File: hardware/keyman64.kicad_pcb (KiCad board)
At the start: 2 copper layers, 80 x 64.7 mm, 33 parts, among them J1 POWER, P1 COMPUTER, P2 KEYBOARD, P3 USB, P4 SERIAL, P5 CONTROL, SW1 RESET, SW2 BOOT, U1 MT8808, U2 ATMEGA1284P-PU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

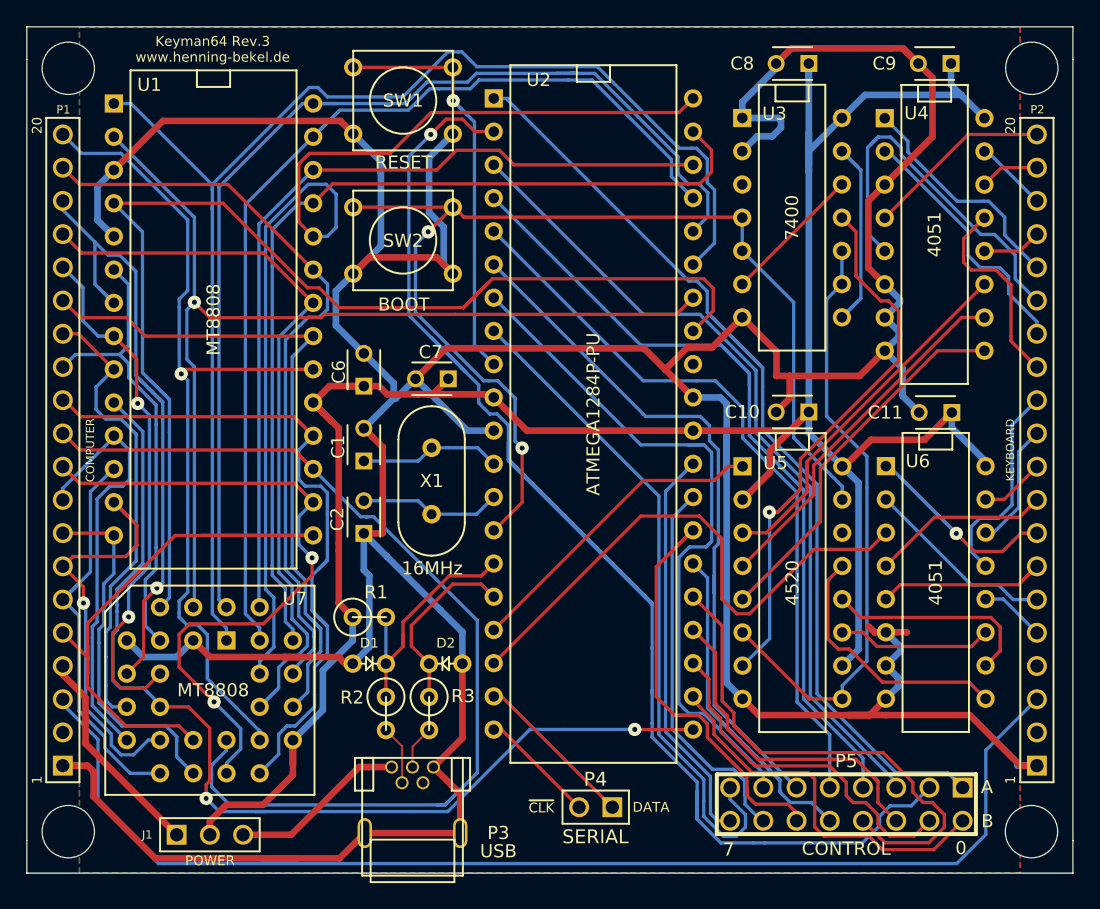
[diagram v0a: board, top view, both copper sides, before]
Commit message: Hardware: Fixed wrong USB level conversion circuit
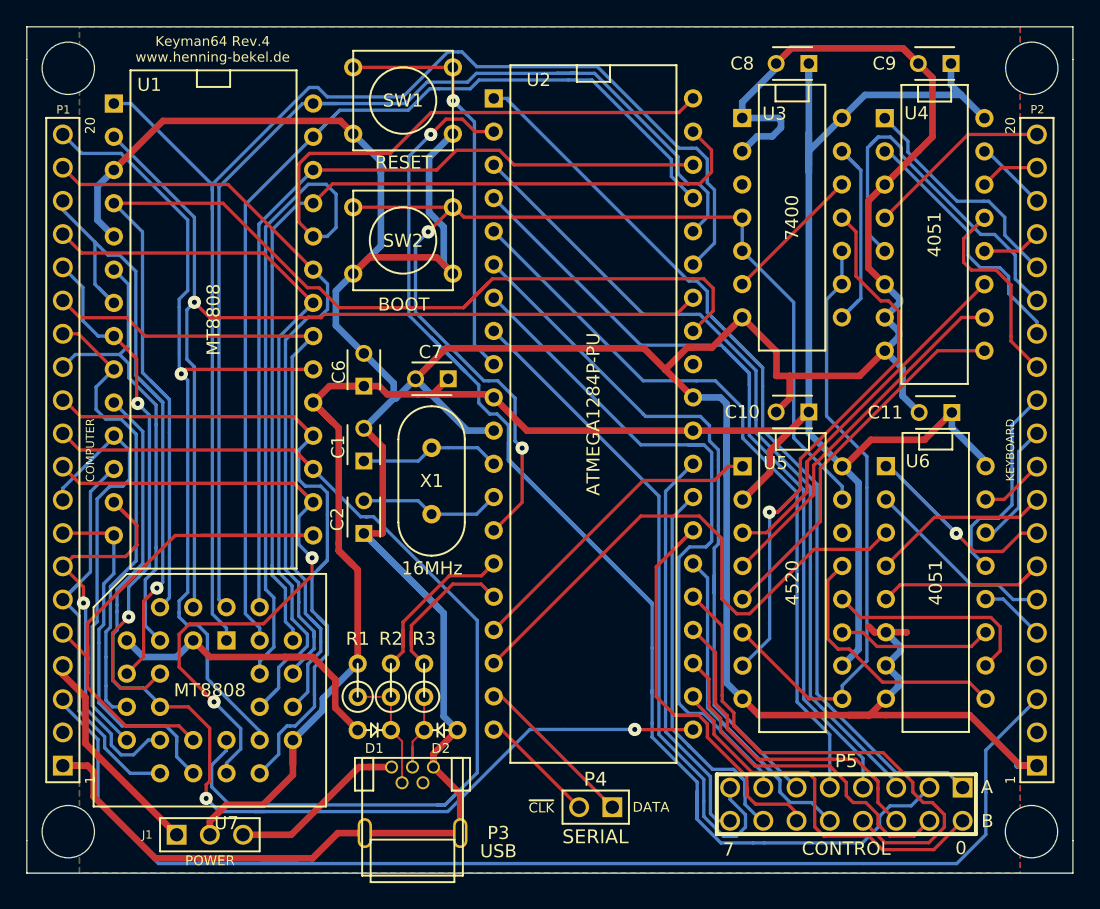
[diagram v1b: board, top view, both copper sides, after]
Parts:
- R1, R2, R3: footprint Discret:R1 -> Diode:R1
- U7: footprint Diode:PLCC28 -> Sockets:PLCC28
- moved D1 5.09 mm to (131.2, 120.1)
- moved D2 5.09 mm to (136.3, 120.1)
- moved R1 4.91 mm to (129.9, 116.3), turned to 90 degrees
- moved R2 2.57 mm to (132.5, 116.3), turned to 90 degrees
- moved R3 2.57 mm to (135.0, 116.3), turned to 90 degrees
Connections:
- D1 pad 1: Net-(D1-Pad1) -> /D-
- D2 pad 1: Net-(D2-Pad1) -> /D+
- R1 pad 1: VCC -> /D-
- R1 pad 2: Net-(D1-Pad1) -> VCC
- R2 pad 1: Net-(D1-Pad1) -> /D-
- R2 pad 2: /D- -> Net-(R2-Pad2)
- R3 pad 1: Net-(D2-Pad1) -> /D+
- R3 pad 2: /D+ -> Net-(R3-Pad2)
- U2 pad 15: Net-(D1-Pad1) -> Net-(R2-Pad2)
- U2 pad 16: Net-(D2-Pad1) -> Net-(R3-Pad2)
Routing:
- net Net-(D1-Pad1): track 19.4 -> 0.00 mm
- net Net-(R2-Pad2): track 0.00 -> 14.3 mm
- net Net-(D2-Pad1): track 14.0 -> 0.00 mm
- net Net-(R3-Pad2): track 0.00 -> 12.4 mm
- net /D-: track 4.53 -> 12.2 mm
- net /D+: track 3.35 -> 7.29 mm
- net GND: track 369.9 -> 372.1 mm
- net VCC: track 184.6 -> 186.5 mm
- net /A7: track 68.6 -> 67.8 mm
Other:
- board text added: "Keyman64 Rev.4 www.henning-bekel.de"
- board text removed: "Keyman64 Rev.3 www.henning-bekel.de"

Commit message: Hardware: Routed USBVCC to socket on the bottom layer to avoid possible strain
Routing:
- net /UVCC: track 13.5 -> 13.9 mm, vias 0 -> 1
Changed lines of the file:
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@@
-(kicad_pcb (version 4) (host pcbnew 4.0.2-stable)
+(kicad_pcb (version 4) (host pcbnew 4.0.1-stable)
   (general
     (links 171)
     (no_connects 0)
-    (area 104.572599 66.320199 184.657201 131.126701)
+    (area 103.263999 57.436901 199.058799 135.5215)
     (thickness 1.6)
     (drawings 23)
-    (tracks 1252)
+    (tracks 1256)
     (zones 0)
     (modules 33)
@@
   (segment (start 157.433348 127.076) (end 156.89072 126.533372) (width 0.254) (layer B.Cu) (net 71))
   (segment (start 154.1399 101.206) (end 155.562 99.7839) (width 0.254) (layer B.Cu) (net 71))
-  (segment (start 121.158 128.143) (end 124.841 128.143) (width 0.508) (layer F.Cu) (net 72))
-  (segment (start 124.841 128.143) (end 130.018 122.966) (width 0.508) (layer F.Cu) (net 72))
-  (segment (start 130.81 122.966) (end 130.018 122.966) (width 0.508) (layer F.Cu) (net 72))
-  (segment (start 132.512 122.966) (end 130.81 122.966) (width 0.508) (layer F.Cu) (net 72))
+  (segment (start 128.397 124.968) (end 130.51 124.968) (width 0.508) (layer B.Cu) (net 72))
+  (segment (start 130.51 124.968) (end 132.512 122.966) (width 0.508) (layer B.Cu) (net 72) (status 800000))
+  (segment (start 121.158 128.143) (end 122.555 128.143) (width 0.508) (layer F.Cu) (net 72) (status 400000))
+  (via (at 125.73 124.968) (size 1.016) (drill 0.381) (layers F.Cu B.Cu) (net 72))
+  (segment (start 125.73 124.968) (end 128.397 124.968) (width 0.508) (layer B.Cu) (net 72))
+  (segment (start 122.555 128.143) (end 125.73 124.968) (width 0.508) (layer F.Cu) (net 72))
+  (segment (start 132.512 123.139) (end 132.512 122.966) (width 0.508) (layer B.Cu) (net 72))
+  (segment (start 132.304 122.966) (end 132.512 122.966) (width 0.508) (layer B.Cu) (net 72))
   (segment (start 134.31012 126.37008) (end 136.811624 126.37008) (width 0.254) (layer B.Cu) (net 73))
   (segment (start 136.811624 126.37008) (end 143.090504 120.0912) (width 0.254) (layer B.Cu) (net 73))
@@
   (segment (start 107.378 118.295624) (end 107.378 117.7798) (width 0.254) (layer B.Cu) (net 76))
   (segment (start 136.4934 111.2074) (end 136.4934 119.0944) (width 0.508) (layer B.Cu) (net 77))
-  (segment (start 136.4934 119.0944) (end 137.541 120.142) (width 0.508) (layer B.Cu) (net 77) (status 800000))
-  (segment (start 136.4934 111.2074) (end 130.391 105.105) (width 0.508) (layer B.Cu) (net 77) (status 800000))
-  (segment (start 135.712 122.966) (end 135.712 121.971) (width 0.508) (layer F.Cu) (net 77) (status 400000))
-  (segment (start 135.712 121.971) (end 137.541 120.142) (width 0.508) (layer F.Cu) (net 77) (status 800000))
+  (segment (start 136.4934 119.0944) (end 137.541 120.142) (width 0.508) (layer B.Cu) (net 77))
+  (segment (start 136.4934 111.2074) (end 130.391 105.105) (width 0.508) (layer B.Cu) (net 77))
+  (segment (start 135.712 122.966) (end 135.712 121.971) (width 0.508) (layer F.Cu) (net 77))
+  (segment (start 135.712 121.971) (end 137.541 120.142) (width 0.508) (layer F.Cu) (net 77))
   (segment (start 128.2065 116.586) (end 128.2065 118.4275) (width 0.508) (layer F.Cu) (net 77))
-  (segment (start 128.2065 118.4275) (end 129.921 120.142) (width 0.508) (layer F.Cu) (net 77) (status 800000))
+  (segment (start 128.2065 118.4275) (end 129.921 120.142) (width 0.508) (layer F.Cu) (net 77))
   (segment (start 130.462 128.016) (end 128.397 128.016) (width 0.508) (layer F.Cu) (net 77))
   (segment (start 128.397 128.016) (end 126.4607 129.9523) (width 0.508) (layer F.Cu) (net 77))

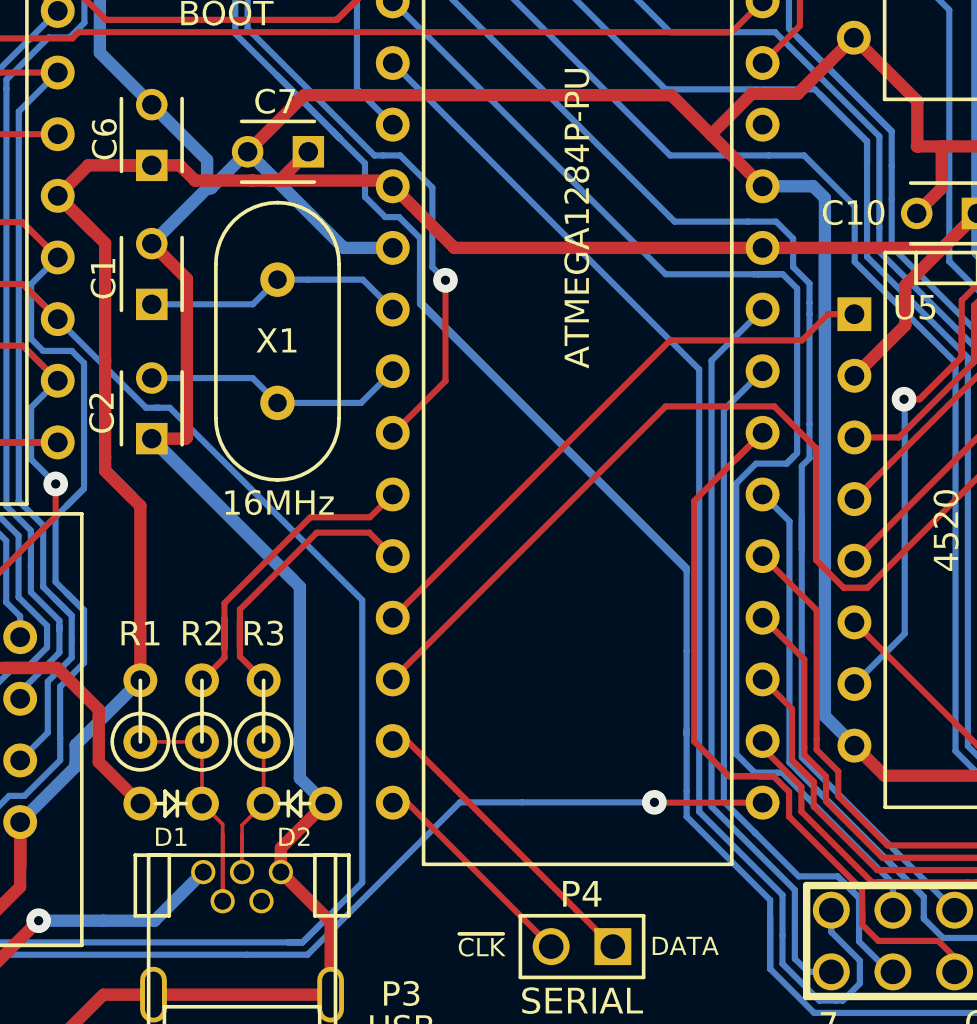
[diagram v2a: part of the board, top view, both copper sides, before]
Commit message: Hardware: Improved routing at ground pads (thermal properties)
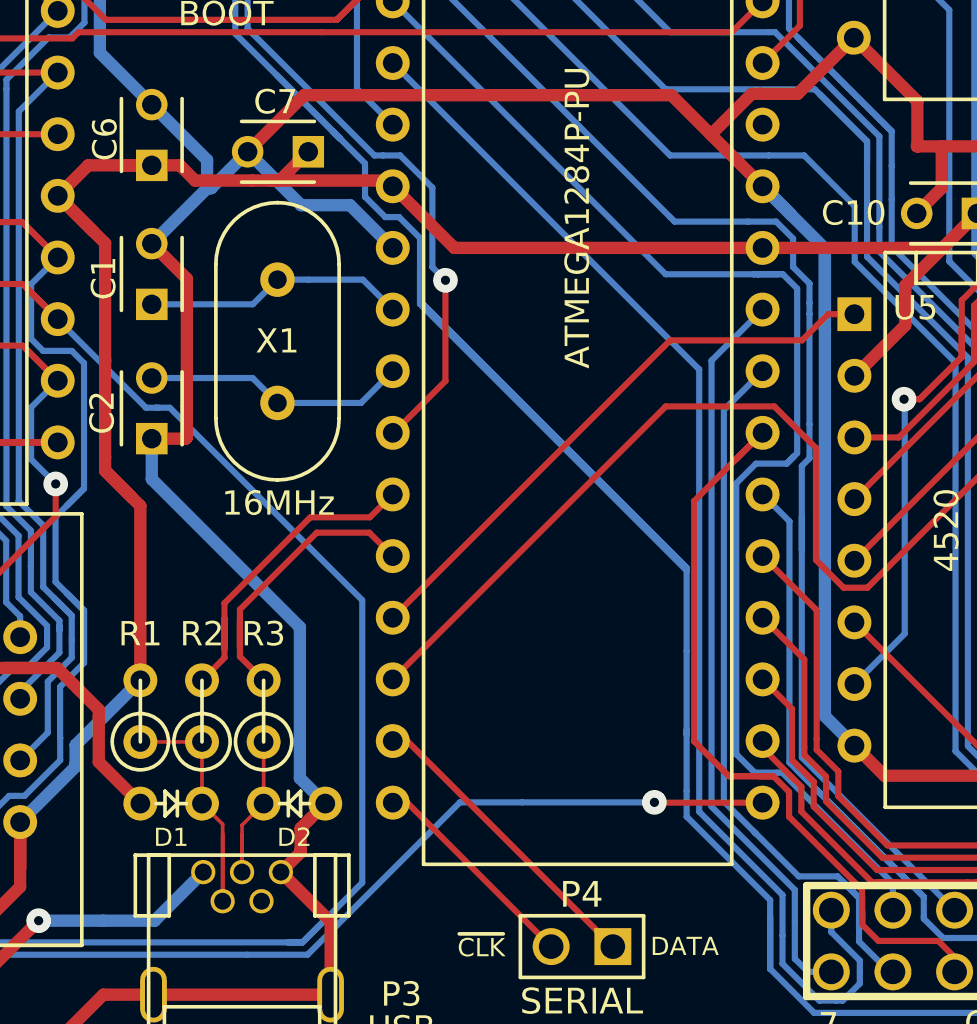
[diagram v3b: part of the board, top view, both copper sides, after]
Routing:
- net GND: track 372.1 -> 363.8 mm
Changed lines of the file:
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@@
-(kicad_pcb (version 4) (host pcbnew 4.0.1-stable)
+(kicad_pcb (version 4) (host pcbnew 4.0.2-stable)
   (general
     (links 171)
     (no_connects 0)
-    (area 103.263999 57.436901 199.058799 135.5215)
+    (area 104.572599 66.320199 184.657201 131.126701)
     (thickness 1.6)
-    (drawings 23)
-    (tracks 1256)
+    (drawings 22)
+    (tracks 1260)
     (zones 0)
     (modules 33)
@@
   )
   (gr_line (start 118.618 113.284) (end 118.618 129.54) (angle 90) (layer Dwgs.User) (width 0.2))
-  (gr_line (start 133.7056 106.9848) (end 133.6548 106.9848) (angle 90) (layer Dwgs.User) (width 0.2))
   (gr_text 20 (at 179.832 73.914 90) (layer F.SilkS)
     (effects (font (size 0.75 0.75) (thickness 0.15)))
@@
   (segment (start 154.1399 101.206) (end 155.562 99.7839) (width 0.254) (layer B.Cu) (net 71))
   (segment (start 128.397 124.968) (end 130.51 124.968) (width 0.508) (layer B.Cu) (net 72))
-  (segment (start 130.51 124.968) (end 132.512 122.966) (width 0.508) (layer B.Cu) (net 72) (status 800000))
-  (segment (start 121.158 128.143) (end 122.555 128.143) (width 0.508) (layer F.Cu) (net 72) (status 400000))
+  (segment (start 130.51 124.968) (end 132.512 122.966) (width 0.508) (layer B.Cu) (net 72))
+  (segment (start 125.73 124.968) (end 128.397 124.968) (width 0.508) (layer B.Cu) (net 72))
+  (segment (start 121.158 128.143) (end 122.555 128.143) (width 0.508) (layer F.Cu) (net 72))
   (via (at 125.73 124.968) (size 1.016) (drill 0.381) (layers F.Cu B.Cu) (net 72))
-  (segment (start 125.73 124.968) (end 128.397 124.968) (width 0.508) (layer B.Cu) (net 72))
   (segment (start 122.555 128.143) (end 125.73 124.968) (width 0.508) (layer F.Cu) (net 72))
   (segment (start 132.512 123.139) (end 132.512 122.966) (width 0.508) (layer B.Cu) (net 72))
@@
   (segment (start 107.378 117.7798) (end 107.378 118.295048) (width 0.254) (layer B.Cu) (net 76))
   (segment (start 107.378 118.295624) (end 107.378 117.7798) (width 0.254) (layer B.Cu) (net 76))
-  (segment (start 136.4934 111.2074) (end 136.4934 119.0944) (width 0.508) (layer B.Cu) (net 77))
+  (segment (start 130.391 105.105) (end 130.391 106.769) (width 0.508) (layer B.Cu) (net 77) (status 400000))
+  (segment (start 136.4934 112.8714) (end 136.4934 119.0944) (width 0.508) (layer B.Cu) (net 77))
+  (segment (start 130.391 106.769) (end 136.4934 112.8714) (width 0.508) (layer B.Cu) (net 77))
+  (segment (start 158.13 99.949) (end 158.13 97.2719) (width 0.508) (layer B.Cu) (net 77))
+  (segment (start 158.13 97.2719) (end 155.562 94.7039) (width 0.508) (layer B.Cu) (net 77) (status 800000))
+  (segment (start 156.7431 95.885) (end 155.562 94.7039) (width 0.508) (layer B.Cu) (net 77) (status 800000))
+  (segment (start 136.54475 95.48425) (end 138.56235 95.48425) (width 0.508) (layer B.Cu) (net 77))
+  (segment (start 138.56235 95.48425) (end 140.322 97.2439) (width 0.508) (layer B.Cu) (net 77) (status 800000))
+  (segment (start 137.541 120.142) (end 136.906 120.777) (width 0.508) (layer F.Cu) (net 77) (status 400000))
+  (segment (start 136.525 121.158) (end 136.525 122.153) (width 0.508) (layer F.Cu) (net 77))
+  (segment (start 136.906 120.777) (end 136.525 121.158) (width 0.508) (layer F.Cu) (net 77))
+  (segment (start 136.525 122.153) (end 136.525 122.047) (width 0.508) (layer F.Cu) (net 77))
+  (segment (start 136.525 122.047) (end 136.525 122.153) (width 0.508) (layer F.Cu) (net 77))
+  (segment (start 136.525 122.153) (end 135.712 122.966) (width 0.508) (layer F.Cu) (net 77))
   (segment (start 136.4934 119.0944) (end 137.541 120.142) (width 0.508) (layer B.Cu) (net 77))
-  (segment (start 136.4934 111.2074) (end 130.391 105.105) (width 0.508) (layer B.Cu) (net 77))
-  (segment (start 135.712 122.966) (end 135.712 121.971) (width 0.508) (layer F.Cu) (net 77))
-  (segment (start 135.712 121.971) (end 137.541 120.142) (width 0.508) (layer F.Cu) (net 77))
   (segment (start 128.2065 116.586) (end 128.2065 118.4275) (width 0.508) (layer F.Cu) (net 77))
   (segment (start 128.2065 118.4275) (end 129.921 120.142) (width 0.508) (layer F.Cu) (net 77))
   (segment (start 130.462 128.016) (end 128.397 128.016) (width 0.508) (layer F.Cu) (net 77))
   (segment (start 128.397 128.016) (end 126.4607 129.9523) (width 0.508) (layer F.Cu) (net 77))
-  (segment (start 135.712 122.966) (end 135.712 122.352) (width 0.508) (layer F.Cu) (net 77))
   (segment (start 128.2065 116.2685) (end 128.2065 116.586) (width 0.508) (layer F.Cu) (net 77))
   (segment (start 126.492 114.554) (end 127.381 115.443) (width 0.508) (layer F.Cu) (net 77))
@@
   (segment (start 123.19 129.9523) (end 126.4607 129.9523) (width 0.508) (layer F.Cu) (net 77))
   (segment (start 130.43406 128.04394) (end 130.462 128.016) (width 0.508) (layer F.Cu) (net 77))
-  (segment (start 136.2456 110.9596) (end 132.15 106.864) (width 0.508) (layer B.Cu) (net 77))
-  (segment (start 132.15 106.864) (end 130.391 105.105) (width 0.508) (layer B.Cu) (net 77))
   (segment (start 122.67184 129.9523) (end 123.19 129.9523) (width 0.508) (layer F.Cu) (net 77))
   (segment (start 123.19 129.9523) (end 125.24658 129.9523) (width 0.508) (layer F.Cu) (net 77))
@@
   (segment (start 131.83616 105.05908) (end 131.83616 103.75392) (width 0.508) (layer F.Cu) (net 77))
   (segment (start 130.391 105.105) (end 130.48508 105.105) (width 0.508) (layer F.Cu) (net 77))
-  (segment (start 158.13 100.61448) (end 158.13 95.187668) (width 0.508) (layer B.Cu) (net 77))
-  (segment (start 158.13 95.187668) (end 157.646232 94.7039) (width 0.508) (layer B.Cu) (net 77))
-  (segment (start 157.646232 94.7039) (end 155.562 94.7039) (width 0.508) (layer B.Cu) (net 77))
+  (segment (start 158.13 100.61448) (end 158.13 99.949) (width 0.508) (layer B.Cu) (net 77))
   (segment (start 159.347 117.754) (end 159.346602 117.754) (width 0.508) (layer B.Cu) (net 77))
   (segment (start 159.346602 117.754) (end 158.13 116.537398) (width 0.508) (layer B.Cu) (net 77))
@@
   (segment (start 159.322 72.1357) (end 161.914 69.5437) (width 0.508) (layer B.Cu) (net 77))
   (segment (start 159.322 73.3425) (end 159.322 72.1357) (width 0.508) (layer B.Cu) (net 77))
-  (segment (start 138.3044 97.2439) (end 134.342 93.2815) (width 0.508) (layer B.Cu) (net 77))
-  (segment (start 140.322 97.2439) (end 138.3044 97.2439) (width 0.508) (layer B.Cu) (net 77))
+  (segment (start 136.54475 95.48425) (end 134.342 93.2815) (width 0.508) (layer B.Cu) (net 77))
   (segment (start 113.538 114.554) (end 112.268 113.284) (width 0.508) (layer B.Cu) (net 77))
   (segment (start 116.078 114.554) (end 113.538 114.554) (width 0.508) (layer B.Cu) (net 77))
